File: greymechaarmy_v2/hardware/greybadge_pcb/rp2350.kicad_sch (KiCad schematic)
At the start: 35 parts, among them J5 USB_C_Receptacle_USB2.0, SW10 SW_Push, SW9 SW_Push, U6 W25Q128JVS, U7 RP2350_60QFN, Y1 12Mhz

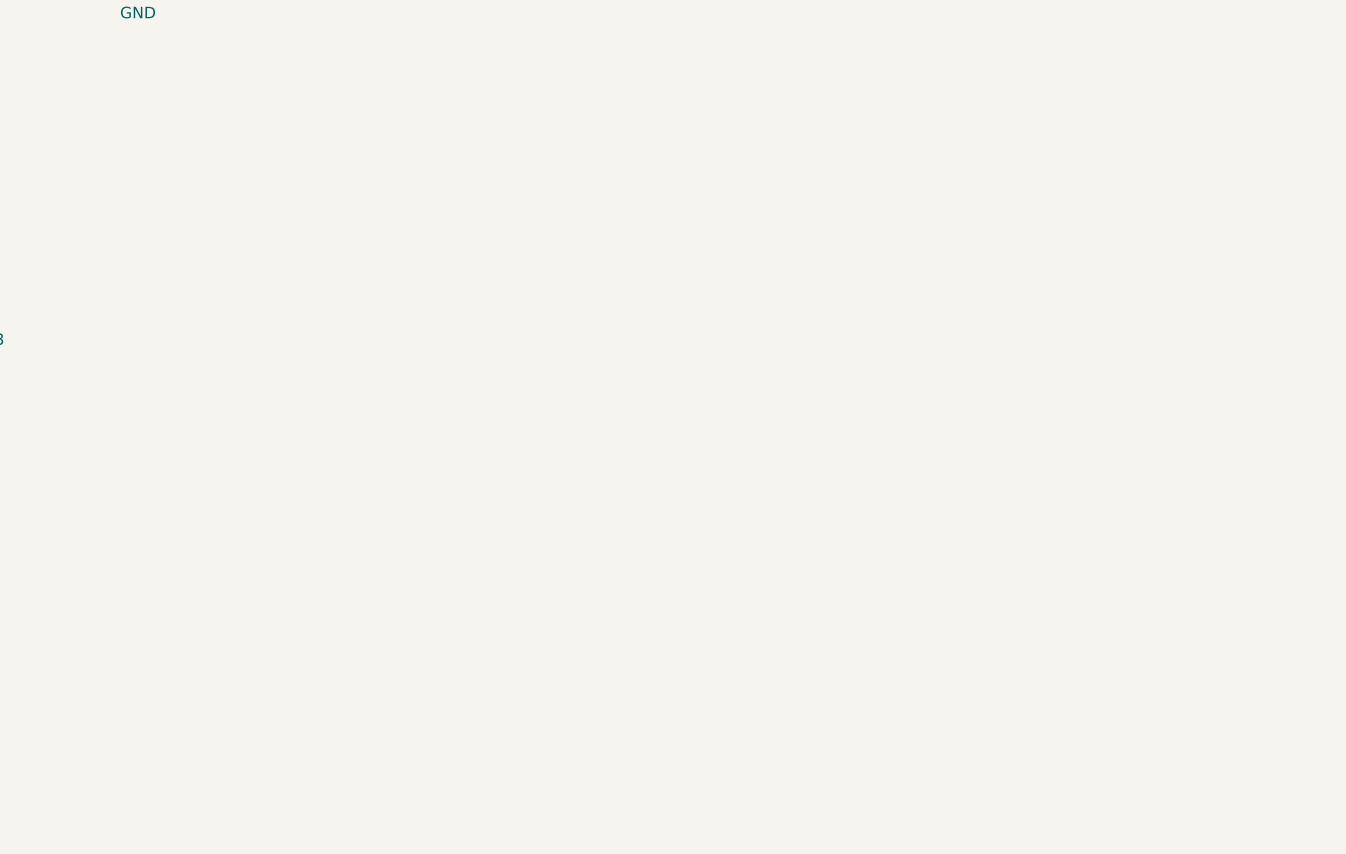
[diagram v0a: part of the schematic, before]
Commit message: feat: PSRAM Schematic addition
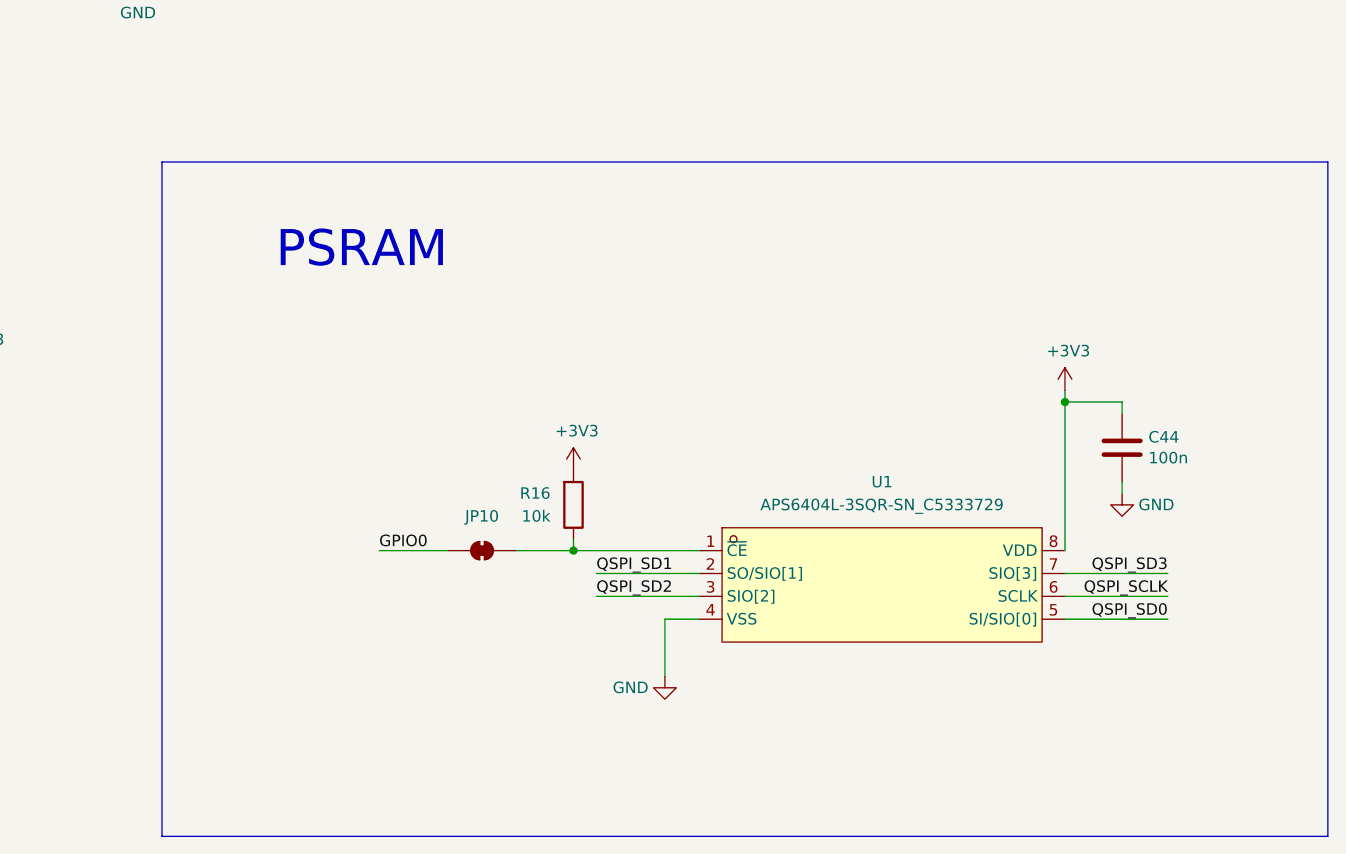
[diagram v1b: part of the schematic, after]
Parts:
- added C44: 100n, Capacitor_SMD:C_0402_1005Metric, symbol Device:C
- added JP10: SolderJumper_2_Bridged, Jumper:SolderJumper-2_P1.3mm_Bridged2Bar_RoundedPad1.0x1.5mm, symbol Jumper:SolderJumper_2_Bridged
- added R16: 10k, Resistor_SMD:R_0603_1608Metric_Pad0.98x0.95mm_HandSolder, symbol Device:R
- added U1: APS6404L-3SQR-SN_C5333729, easyeda2kicad:SOIC-8_L4.9-W3.9-P1.27-LS6.0-BL, symbol easyeda2kicad:APS6404L-3SQR-SN_C5333729
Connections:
- net +3V3: now also C44.1, R16.2, U1.8 (VDD)
- net GND: now also C44.2, U1.4 (VSS)
- net GPIO0: now also JP10.1 (A)
- net QSPI_SCLK: now also U1.6 (SCLK)
- net QSPI_SD0: now also U1.5 (SI/SIO[0])
- net QSPI_SD1: now also U1.2 (SO/SIO[1])
- net QSPI_SD2: now also U1.3 (SIO[2])
- net QSPI_SD3: now also U1.7 (SIO[3])
- new net: JP10.2 (B), R16.1, U1.1 (~{CE})
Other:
- note added: "PSRAM"
